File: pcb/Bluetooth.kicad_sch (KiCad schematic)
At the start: 18 parts, among them U12 RN4678

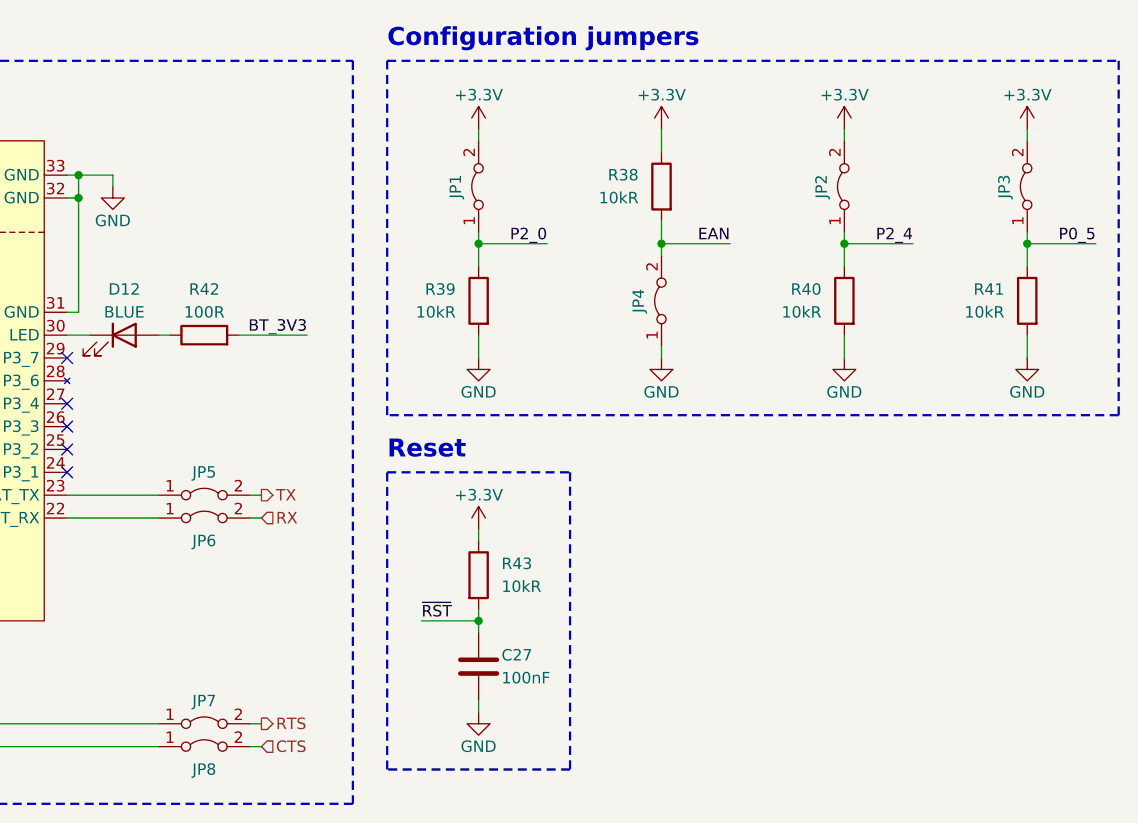
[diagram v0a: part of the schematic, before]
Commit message: [pcb] Trying to minimize number of vias
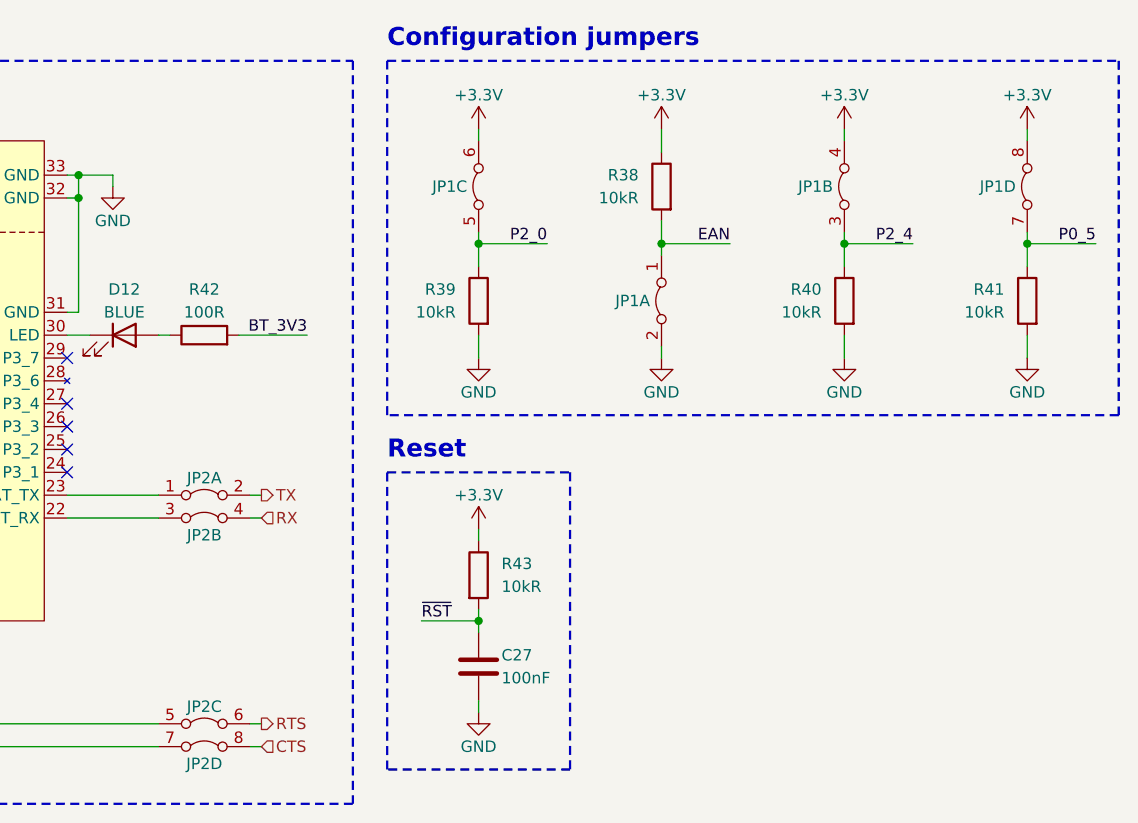
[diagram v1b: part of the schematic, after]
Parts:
- removed JP1, JP2, JP3, JP4, JP5, JP6, JP7, JP8: Jumper_2_Bridged, Connector_PinHeader_2.54mm:PinHeader_1x02_P2.54mm_Vertical, symbol Jumper:Jumper_2_Bridged
- added JP1, JP2: Jumper_x4_Bridged, Connector_PinHeader_2.54mm:PinHeader_2x04_P2.54mm_Vertical, symbol Autko:Jumper_x4_Bridged
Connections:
- net +3.3V: now also JP1.4, JP1.6, JP1.8
- net CTS: now also JP2.8
- net EAN: now also JP1.1
- net GND: now also JP1.2
- net P0_5: now also JP1.7
- net P2_0: now also JP1.5
- net P2_4: now also JP1.3
- net RTS: now also JP2.6
- net RX: now also JP2.4
- net TX: now also JP2.2
- net at U12.15 (P1_7/CTS): now also JP2.7
- net at U12.17 (P0_0/RTS): now also JP2.5
- net at U12.22 (UART_RX): now also JP2.3
- net at U12.23 (UART_TX): now also JP2.1

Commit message: [pcb] BT routing
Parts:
- added C25: 100nF, Capacitor_SMD:C_0805_2012Metric, symbol Device:C
- added U12: 74HC14, Package_SO:TSSOP-14_4.4x5mm_P0.65mm, symbol 74xx:74HC14
- renumbered C26 to C24, C27 to C26, D12 to D11, R38 to R37, R40 to R38, R41 to R40, R42 to R41, R43 to R42, U12 to U13
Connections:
- net +3.3V: now also R38.1, R39.1, R40.1, C25.1, U12.14 (VCC); no longer JP1.4, JP1.6, JP1.8
- net EAN: now also U12.6; no longer JP1.1, R37.2
- net GND: now also JP1.4, JP1.6, JP1.8, C25.2, U12.13, U12.7 (GND); no longer R38.2, R39.2, R40.2
- net P0_5: now also U12.8; no longer JP1.7, R40.1
- net P2_0: now also U12.10; no longer JP1.5, R39.1
- net P2_4: now also U12.2; no longer JP1.3, R38.1
- new net: JP1.1, R37.2, U12.3
- new net: JP1.3, R38.2, U12.1
- new net: JP1.5, R39.2, U12.11
- new net: U12.4, U12.5
- new net: JP1.7, R40.2, U12.9
- no-connect marks 12 -> 13
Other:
- moved on the sheet: JP1A, JP1B, JP1C, JP1D, R37, R38, R39, R40

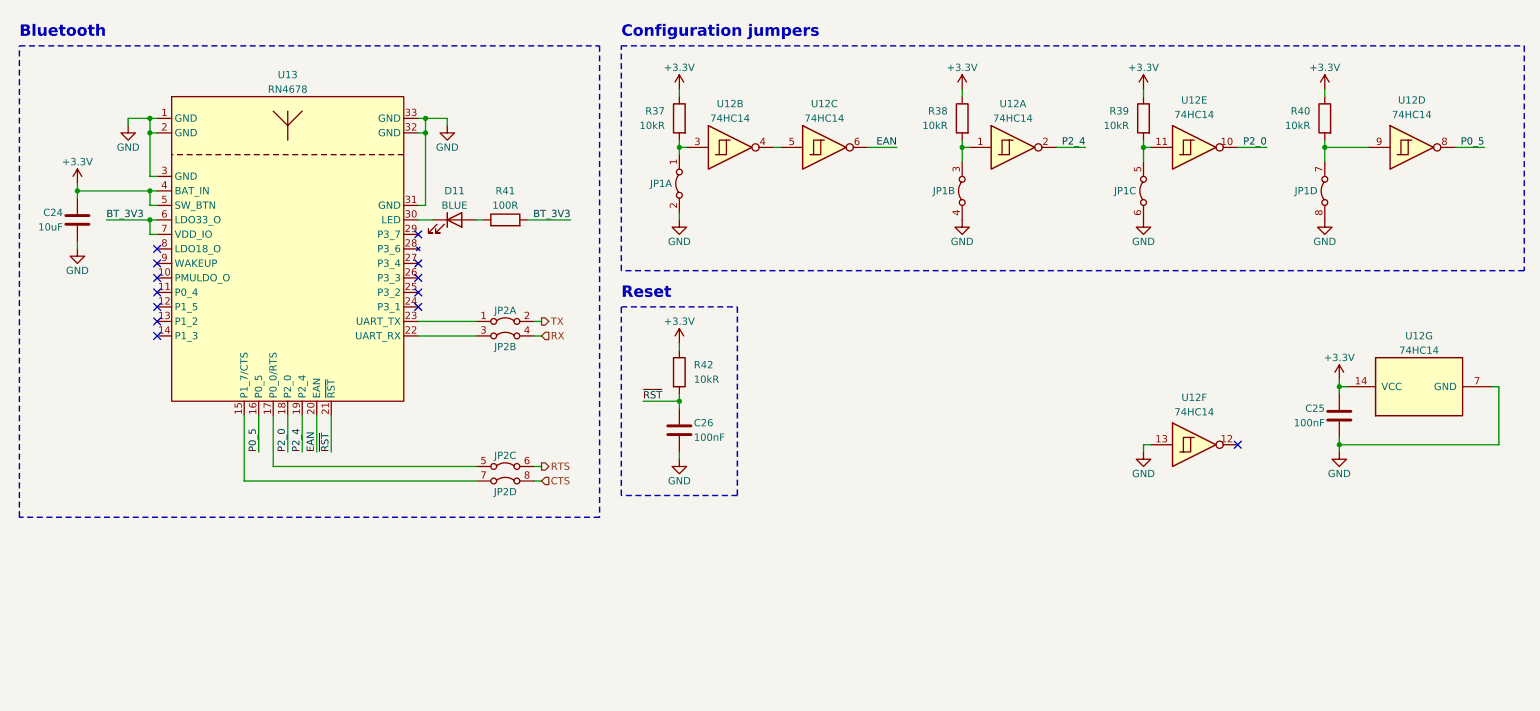
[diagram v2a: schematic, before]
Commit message: [pcb] 4 layer PCB
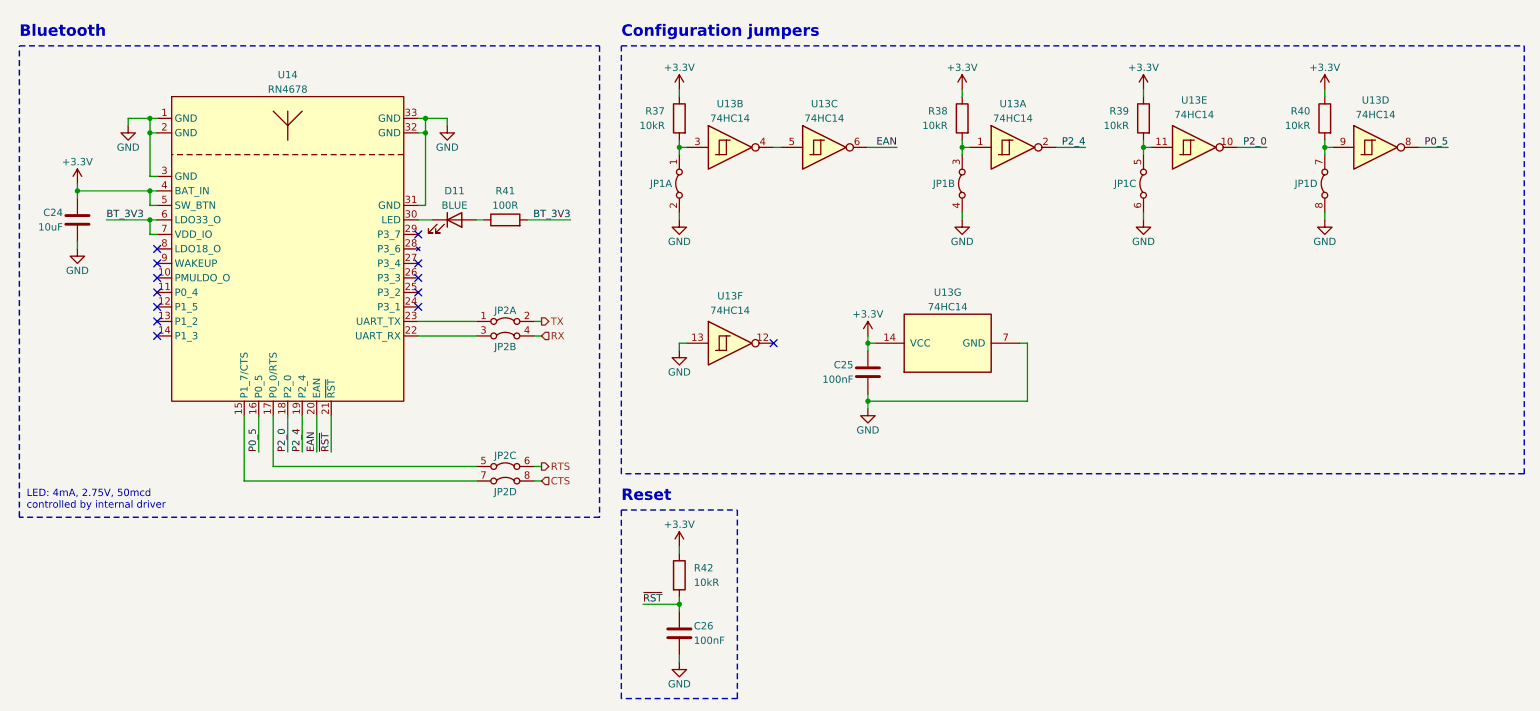
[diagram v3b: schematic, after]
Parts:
- renumbered U12 to U13, U13 to U14
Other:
- note added: "LED: 4mA, 2.75V, 50mcd controlled by internal driver"
- moved on the sheet: C25, C26, JP1B, JP1C, JP1D, R42, U13D, U13F, U13G

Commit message: [pcb] BT config rework
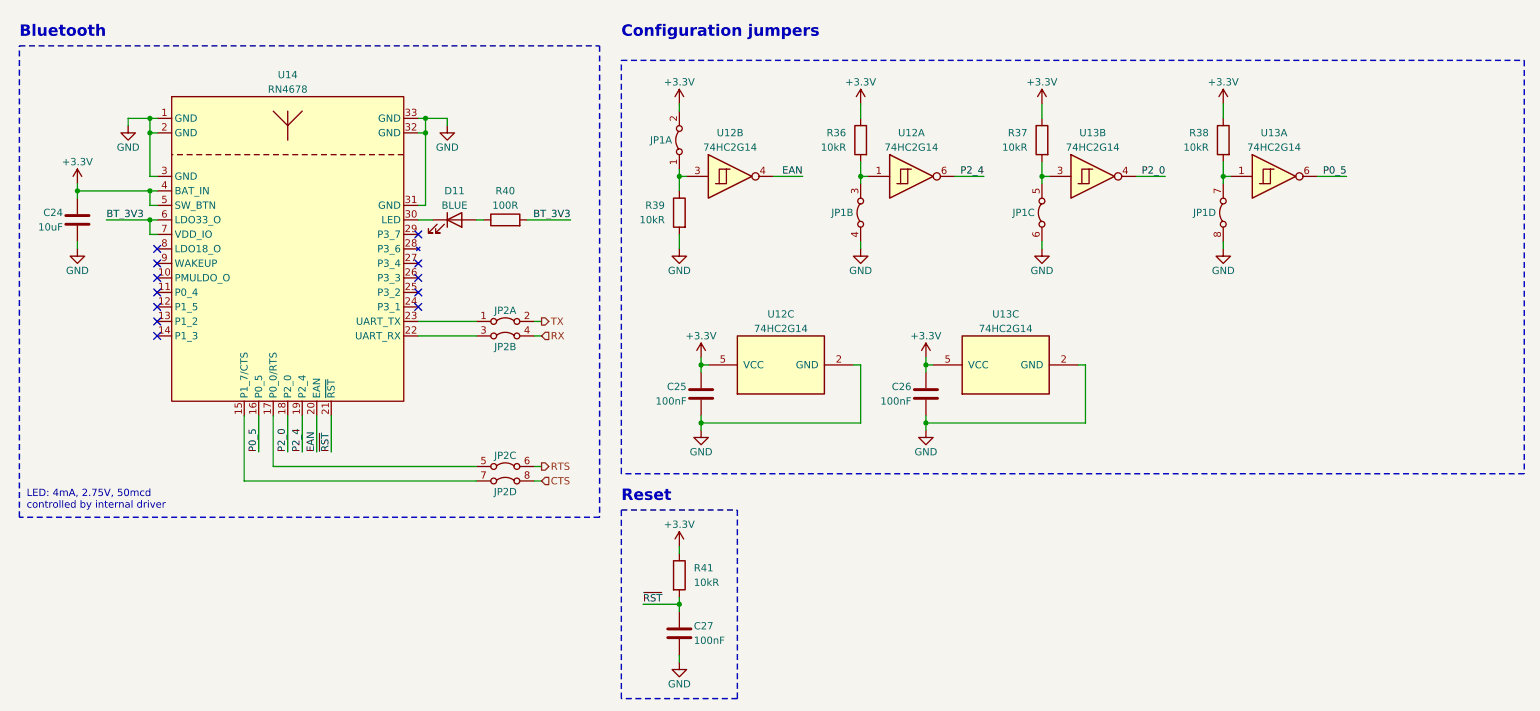
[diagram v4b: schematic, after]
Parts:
- removed U13: 74HC14, Package_SO:TSSOP-14_4.4x5mm_P0.65mm, symbol 74xx:74HC14
- added C26: 100nF, Capacitor_SMD:C_0805_2012Metric, symbol Device:C
- added U12, U13: 74HC2G14, Package_TO_SOT_SMD:SOT-363_SC-70-6, symbol Autko:74HC2G14
- renumbered C26 to C27, R38 to R36, R39 to R37, R40 to R38, R37 to R39, R41 to R40, R42 to R41
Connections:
- net +3.3V: now also JP1.2, C26.1, U12.5 (VCC), U13.5 (VCC); no longer R39.1
- net EAN: now also U12.4
- net GND: now also R39.2, C26.2, U12.2 (GND), U13.2 (GND); no longer JP1.2
- net P0_5: now also U13.6
- net P2_0: now also U13.4
- net P2_4: now also U12.6
- net at JP1.1: now also R39.1, U12.3; no longer R39.2
- net at JP1.3, R36.2: now also U12.1
- net at JP1.5, R37.2: now also U13.3
- net at JP1.7, R38.2: now also U13.1
- no-connect marks 13 -> 12
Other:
- moved on the sheet: JP1A, JP1B, JP1C, JP1D, R36, R37, R38, R39

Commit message: [pcb] Almost ready
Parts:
- added R41, R42: 330R, Resistor_SMD:R_0805_2012Metric, symbol Device:R
- renumbered R41 to R43
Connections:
- net at JP2.3: now also R42.2; no longer U14.22 (UART_RX)
- net at U14.23 (UART_TX): now also R41.1; no longer JP2.1
- new net: R42.1, U14.22 (UART_RX)
- new net: JP2.1, R41.2
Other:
- moved on the sheet: JP2A, JP2B
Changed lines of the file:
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@@
-    (stroke (width 0) (type default))
-  )
-  (wire (pts (xy 87.63 72.39) (xy 97.79 72.39))
     (stroke (width 0) (type default))
   )
@@
     (stroke (width 0) (type default))
   )
+  (wire (pts (xy 88.9 72.39) (xy 87.63 72.39))
+    (stroke (width 0) (type default))
+  )
   (wire (pts (xy 40.64 44.45) (xy 40.64 36.83))
     (stroke (width 0) (type default))
@@
     (stroke (width 0) (type default))
   )
-  (wire (pts (xy 107.95 69.85) (xy 109.22 69.85))
+  (wire (pts (xy 110.49 68.58) (xy 111.76 68.58))
     (stroke (width 0) (type default))
   )
@@
     (stroke (width 0) (type default))
   )
+  (wire (pts (xy 88.9 73.66) (xy 90.17 73.66))
+    (stroke (width 0) (type default))
+  )
   (wire (pts (xy 41.91 49.53) (xy 40.64 49.53))
     (stroke (width 0) (type default))
@@
     (stroke (width 0) (type default))
   )
+  (wire (pts (xy 88.9 68.58) (xy 90.17 68.58))
+    (stroke (width 0) (type default))
+  )
   (wire (pts (xy 133.35 129.54) (xy 133.35 128.27))
     (stroke (width 0) (type default))
@@
     (stroke (width 0) (type default))
   )
+  (wire (pts (xy 88.9 69.85) (xy 87.63 69.85))
+    (stroke (width 0) (type default))
+  )
   (wire (pts (xy 176.53 87.63) (xy 176.53 88.9))
     (stroke (width 0) (type default))
@@
     (stroke (width 0) (type default))
   )
+  (wire (pts (xy 97.79 73.66) (xy 100.33 73.66))
+    (stroke (width 0) (type default))
+  )
   (wire (pts (xy 87.63 52.07) (xy 90.17 52.07))
     (stroke (width 0) (type default))
@@
     (stroke (width 0) (type default))
   )
+  (wire (pts (xy 97.79 68.58) (xy 100.33 68.58))
+    (stroke (width 0) (type default))
+  )
   (wire (pts (xy 36.83 35.56) (xy 36.83 34.29))
     (stroke (width 0) (type default))
@@
     (stroke (width 0) (type default))
   )
-  (wire (pts (xy 87.63 69.85) (xy 97.79 69.85))
-    (stroke (width 0) (type default))
-  )
   (wire (pts (xy 87.63 49.53) (xy 88.9 49.53))
     (stroke (width 0) (type default))
@@
     (stroke (width 0) (type default))
   )
+  (wire (pts (xy 88.9 68.58) (xy 88.9 69.85))
+    (stroke (width 0) (type default))
+  )
   (wire (pts (xy 228.6 44.45) (xy 229.87 44.45))
     (stroke (width 0) (type default))
@@
     (stroke (width 0) (type default))
   )
+  (wire (pts (xy 88.9 73.66) (xy 88.9 72.39))
+    (stroke (width 0) (type default))
+  )
   (wire (pts (xy 62.23 86.36) (xy 62.23 95.25))
     (stroke (width 0) (type default))
   )
-  (wire (pts (xy 107.95 72.39) (xy 109.22 72.39))
+  (wire (pts (xy 110.49 73.66) (xy 111.76 73.66))
     (stroke (width 0) (type default))
   )
@@
     (stroke (width 0) (type default))
   )
-  (rectangle (start 123.19 24.13) (end 281.305 96.52)
+  (rectangle (start 123.19 24.13) (end 255.27 96.52)
     (stroke (width 0.25) (type dash))
     (fill (type none))
@@
     (effects (font (size 1.27 1.27)) (justify left bottom))
   )
-  (hierarchical_label "RX" (shape input) (at 109.22 72.39 0) (fields_autoplaced)
+  (hierarchical_label "RX" (shape input) (at 111.76 73.66 0) (fields_autoplaced)
     (effects (font (size 1.27 1.27)) (justify left))
   )
@@
     (effects (font (size 1.27 1.27)) (justify left))
   )
-  (hierarchical_label "TX" (shape output) (at 109.22 69.85 0) (fields_autoplaced)
+  (hierarchical_label "TX" (shape output) (at 111.76 68.58 0) (fields_autoplaced)
     (effects (font (size 1.27 1.27)) (justify left))
   )
@@
     )
   )
-  (symbol (lib_id "Autko:Jumper_x4_Bridged") (at 102.87 72.39 0) (unit 2)
-    (in_bom yes) (on_board yes) (dnp no)
-    (property "Reference" "JP2" (at 102.87 74.295 0)
-      (effects (font (size 1.27 1.27)))
-    )
-    (property "Value" "Jumper_x4_Bridged" (at 102.87 76.2 0)
-      (effects (font (size 1.27 1.27)) hide)
-    )
-    (property "Footprint" "Connector_PinHeader_2.54mm:PinHeader_2x04_P2.54mm_Vertical" (at 102.87 74.295 0)
-      (effects (font (size 1.27 1.27)) hide)
-    )
-    (property "Datasheet" "" (at 102.87 72.39 0)
+  (symbol (lib_id "Autko:Jumper_x4_Bridged") (at 105.41 73.66 0) (unit 2)
+    (in_bom yes) (on_board yes) (dnp no)
+    (property "Reference" "JP2" (at 105.41 75.565 0)
+      (effects (font (size 1.27 1.27)))
+    )
+    (property "Value" "Jumper_x4_Bridged" (at 105.41 77.47 0)
+      (effects (font (size 1.27 1.27)) hide)
+    )
+    (property "Footprint" "Connector_PinHeader_2.54mm:PinHeader_2x04_P2.54mm_Vertical" (at 105.41 75.565 0)
+      (effects (font (size 1.27 1.27)) hide)
+    )
+    (property "Datasheet" "" (at 105.41 73.66 0)
       (effects (font (size 1.27 1.27)) hide)
     )
@@
     )
   )
+  (symbol (lib_id "Device:R") (at 93.98 73.66 90) (mirror x) (unit 1)
+    (in_bom yes) (on_board yes) (dnp no)
+    (property "Reference" "R42" (at 93.98 78.74 90)
+      (effects (font (size 1.27 1.27)))
+    )
+    (property "Value" "330R" (at 93.98 76.2 90)
+      (effects (font (size 1.27 1.27)))
+    )
+    (property "Footprint" "Resistor_SMD:R_0805_2012Metric" (at 93.98 71.882 90)
+      (effects (font (size 1.27 1.27)) hide)
+    )
+    (property "Datasheet" "~" (at 93.98 73.66 0)
+      (effects (font (size 1.27 1.27)) hide)
+    )
+    (pin "1")
+    (pin "2")
+    (instances
+      (project "Autko"
+        (path "/8d5cfdec-de34-4148-9100-7125640c46f5/bb9a200c-6921-438f-a82b-708524bb5612"
+          (reference "R42") (unit 1)
+        )
+      )
+    )
+  )
   (symbol (lib_id "Autko:Jumper_x4_Bridged") (at 196.85 50.8 90) (mirror x) (unit 3)
     (in_bom yes) (on_board yes) (dnp no)
@@
     )
   )
-  (symbol (lib_id "Autko:Jumper_x4_Bridged") (at 102.87 69.85 0) (unit 1)
-    (in_bom yes) (on_board yes) (dnp no)
-    (property "Reference" "JP2" (at 102.87 67.945 0)
-      (effects (font (size 1.27 1.27)))
-    )
-    (property "Value" "Jumper_x4_Bridged" (at 102.87 73.66 0)
-      (effects (font (size 1.27 1.27)) hide)
-    )
-    (property "Footprint" "Connector_PinHeader_2.54mm:PinHeader_2x04_P2.54mm_Vertical" (at 102.87 71.755 0)
-      (effects (font (size 1.27 1.27)) hide)
-    )
-    (property "Datasheet" "" (at 102.87 69.85 0)
+  (symbol (lib_id "Autko:Jumper_x4_Bridged") (at 105.41 68.58 0) (unit 1)
+    (in_bom yes) (on_board yes) (dnp no)
+    (property "Reference" "JP2" (at 105.41 66.675 0)
+      (effects (font (size 1.27 1.27)))
+    )
+    (property "Value" "Jumper_x4_Bridged" (at 105.41 72.39 0)
+      (effects (font (size 1.27 1.27)) hide)
+    )
+    (property "Footprint" "Connector_PinHeader_2.54mm:PinHeader_2x04_P2.54mm_Vertical" (at 105.41 70.485 0)
+      (effects (font (size 1.27 1.27)) hide)
+    )
+    (property "Datasheet" "" (at 105.41 68.58 0)
       (effects (font (size 1.27 1.27)) hide)
     )
@@
   (symbol (lib_id "Device:R") (at 133.35 114.3 0) (unit 1)
     (in_bom yes) (on_board yes) (dnp no)
-    (property "Reference" "R41" (at 135.89 113.03 0)
+    (property "Reference" "R43" (at 135.89 113.03 0)
       (effects (font (size 1.27 1.27)) (justify left))
     )
@@
       (project "Autko"
         (path "/8d5cfdec-de34-4148-9100-7125640c46f5/bb9a200c-6921-438f-a82b-708524bb5612"
-          (reference "R41") (unit 1)
+          (reference "R43") (unit 1)
         )
       )
@@
         )
       )
+    )
+  )
+  (symbol (lib_id "Device:R") (at 93.98 68.58 90) (unit 1)
+    (in_bom yes) (on_board yes) (dnp no) (fields_autoplaced)
+    (property "Reference" "R41" (at 93.98 63.5 90)
+      (effects (font (size 1.27 1.27)))
+    )
+    (property "Value" "330R" (at 93.98 66.04 90)
+      (effects (font (size 1.27 1.27)))
+    )
+    (property "Footprint" "Resistor_SMD:R_0805_2012Metric" (at 93.98 70.358 90)
+      (effects (font (size 1.27 1.27)) hide)
+    )
+    (property "Datasheet" "~" (at 93.98 68.58 0)
+      (effects (font (size 1.27 1.27)) hide)
+    )
+    (pin "1")
+    (pin "2")
+    (instances
+      (project "Autko"
+        (path "/8d5cfdec-de34-4148-9100-7125640c46f5/bb9a200c-6921-438f-a82b-708524bb5612"
+          (reference "R41") (unit 1)
+        )
+      )
